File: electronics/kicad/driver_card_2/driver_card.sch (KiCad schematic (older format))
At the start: 27 parts, among them J1 CONN_10SMD_MALE, Q1 2N7002, Q2 MMBT4401, Q3 BSS84, U2 INA194

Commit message: Isoelectric point data
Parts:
- removed R10: 1k, Resistor_SMD:R_0603_1608Metric, symbol SparkFun-Resistors:RESISTOR0402
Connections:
- wire segments 21 -> 20
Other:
- moved on the sheet: C10, Q3, R16, R17, TP4, U2, U?
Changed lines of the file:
@@
 $EndComp
 Wire Wire Line
-	7950 3650 7950 3350
-Wire Wire Line
-	7550 5200 7550 4800
+	7800 3450 7800 3150
+Wire Wire Line
+	7400 5000 7400 4600
 Wire Wire Line
 	4400 5400 4400 5650
@@
 $EndComp
 Wire Wire Line
-	8150 4500 8450 4500
+	8000 4300 8300 4300
 $Comp
 L SparkFun-PowerSymbols:3.3V #SUPPLY0103
@@
 $EndComp
 Wire Wire Line
-	8150 4500 8150 4800
-Connection ~ 8150 4500
-Wire Wire Line
-	8150 4250 8150 4500
+	8000 4300 8000 4600
+Connection ~ 8000 4300
+Wire Wire Line
+	8000 4050 8000 4300
 $Comp
 L SparkFun-Resistors:RESISTOR0402 R17
 U 1 1 5F09ED98
-P 7950 4800
-F 0 "R17" V 7855 4868 45  0000 L CNN
-F 1 "2.2r" V 7939 4868 45  0000 L CNN
-F 2 "Resistor_SMD:R_0805_2012Metric" H 7950 4950 20  0001 C CNN
-F 3 "" H 7950 4800 60  0001 C CNN
-F 4 " " V 8034 4868 60  0000 L CNN "Field4"
-	1    7950 4800
+P 7800 4600
+F 0 "R17" V 7705 4668 45  0000 L CNN
+F 1 "2.2r" V 7789 4668 45  0000 L CNN
+F 2 "Resistor_SMD:R_0805_2012Metric" H 7800 4750 20  0001 C CNN
+F 3 "" H 7800 4600 60  0001 C CNN
+F 4 " " V 7884 4668 60  0000 L CNN "Field4"
+	1    7800 4600
 	-1   0    0    1
 $EndComp
@@
 L power:GND #PWR0115
 U 1 1 5F0715F5
-P 8250 4050
-F 0 "#PWR0115" H 8250 4050 30  0001 C CNN
-F 1 "GND" H 8250 3980 30  0001 C CNN
-F 2 "" H 8250 4050 50  0001 C CNN
-F 3 "" H 8250 4050 50  0001 C CNN
-	1    8250 4050
+P 8100 3850
+F 0 "#PWR0115" H 8100 3850 30  0001 C CNN
+F 1 "GND" H 8100 3780 30  0001 C CNN
+F 2 "" H 8100 3850 50  0001 C CNN
+F 3 "" H 8100 3850 50  0001 C CNN
+	1    8100 3850
 	0    -1   -1   0
 $EndComp
@@
 L SparkFun-PowerSymbols:3.3V #SUPPLY0102
 U 1 1 5F06F21D
-P 7650 4050
-F 0 "#SUPPLY0102" H 7700 4050 45  0001 L BNN
-F 1 "3.3V" V 7650 4178 45  0000 L CNN
-F 2 "" V 7608 4177 60  0000 L CNN
-F 3 "" H 7650 4050 60  0001 C CNN
-	1    7650 4050
+P 7500 3850
+F 0 "#SUPPLY0102" H 7550 3850 45  0001 L BNN
+F 1 "3.3V" V 7500 3978 45  0000 L CNN
+F 2 "" V 7458 3977 60  0000 L CNN
+F 3 "" H 7500 3850 60  0001 C CNN
+	1    7500 3850
 	0    -1   -1   0
 $EndComp
@@
 L power:GND #PWR0112
 U 1 1 5F06BB87
-P 7650 3750
-F 0 "#PWR0112" H 7650 3750 30  0001 C CNN
-F 1 "GND" H 7650 3680 30  0001 C CNN
-F 2 "" H 7650 3750 50  0001 C CNN
-F 3 "" H 7650 3750 50  0001 C CNN
-	1    7650 3750
+P 7500 3550
+F 0 "#PWR0112" H 7500 3550 30  0001 C CNN
+F 1 "GND" H 7500 3480 30  0001 C CNN
+F 2 "" H 7500 3550 50  0001 C CNN
+F 3 "" H 7500 3550 50  0001 C CNN
+	1    7500 3550
 	-1   0    0    1
 $EndComp
@@
 L SparkFun-Capacitors:4.7UF0603 C10
 U 1 1 5F06AAD3
-P 7650 3950
-F 0 "C10" V 7416 4000 45  0000 C CNN
-F 1 "0.1 uF" V 7500 4000 45  0000 C CNN
-F 2 "0603" H 7650 4200 20  0001 C CNN
-F 3 "" H 7650 3950 50  0001 C CNN
-F 4 "" H 7758 3916 60  0000 L CNN "Field4"
-	1    7650 3950
-	1    0    0    -1
-$EndComp
-Wire Wire Line
-	7750 4250 7850 4250
-Wire Wire Line
-	8150 4250 8050 4250
-Connection ~ 7650 4050
+P 7500 3750
+F 0 "C10" V 7266 3800 45  0000 C CNN
+F 1 "0.1 uF" V 7350 3800 45  0000 C CNN
+F 2 "0603" H 7500 4000 20  0001 C CNN
+F 3 "" H 7500 3750 50  0001 C CNN
+F 4 "" H 7608 3716 60  0000 L CNN "Field4"
+	1    7500 3750
+	1    0    0    -1
+$EndComp
+Wire Wire Line
+	7600 4050 7700 4050
+Wire Wire Line
+	8000 4050 7900 4050
+Connection ~ 7500 3850
 $Comp
 L Amplifier_Current:INA194 U2
 U 1 1 5F064800
-P 7950 3950
-F 0 "U2" H 8294 3996 50  0000 L CNN
-F 1 "INA194" H 8294 3905 50  0000 L CNN
-F 2 "Package_TO_SOT_SMD:SOT-23-5" H 7950 3950 50  0001 C CNN
-F 3 "http://www.ti.com/lit/ds/symlink/ina193.pdf" H 7950 3950 50  0001 C CNN
-	1    7950 3950
+P 7800 3750
+F 0 "U2" H 8144 3796 50  0000 L CNN
+F 1 "INA194" H 8144 3705 50  0000 L CNN
+F 2 "Package_TO_SOT_SMD:SOT-23-5" H 7800 3750 50  0001 C CNN
+F 3 "http://www.ti.com/lit/ds/symlink/ina193.pdf" H 7800 3750 50  0001 C CNN
+	1    7800 3750
 	0    -1   -1   0
 $EndComp
@@
 $EndComp
 Wire Wire Line
-	7750 4800 7750 4500
-Wire Wire Line
-	7750 4500 7750 4250
-Connection ~ 7750 4500
+	7600 4600 7600 4300
+Wire Wire Line
+	7600 4300 7600 4050
+Connection ~ 7600 4300
 $Comp
 L SparkFun-Resistors:RESISTOR0402 R16
 U 1 1 5F048AA5
-P 7950 4500
-F 0 "R16" V 7855 4568 45  0000 L CNN
-F 1 "2.2r" V 7939 4568 45  0000 L CNN
-F 2 "Resistor_SMD:R_0805_2012Metric" H 7950 4650 20  0001 C CNN
-F 3 "" H 7950 4500 60  0001 C CNN
-F 4 " " V 8034 4568 60  0000 L CNN "Field4"
-	1    7950 4500
+P 7800 4300
+F 0 "R16" V 7705 4368 45  0000 L CNN
+F 1 "2.2r" V 7789 4368 45  0000 L CNN
+F 2 "Resistor_SMD:R_0805_2012Metric" H 7800 4450 20  0001 C CNN
+F 3 "" H 7800 4300 60  0001 C CNN
+F 4 " " V 7884 4368 60  0000 L CNN "Field4"
+	1    7800 4300
 	-1   0    0    1
 $EndComp
@@
 $EndComp
 Connection ~ 6450 1800
-$Comp
-L SparkFun-Resistors:RESISTOR0402 R10
-U 1 1 5EF918DB
-P 6250 1800
-F 0 "R10" V 6345 1732 45  0000 R CNN
-F 1 "1k" V 6261 1732 45  0000 R CNN
-F 2 "Resistor_SMD:R_0603_1608Metric" H 6250 1950 20  0001 C CNN
-F 3 "" H 6250 1800 60  0001 C CNN
-F 4 " " V 6166 1732 60  0000 R CNN "Field4"
-	1    6250 1800
-	-1   0    0    1
-$EndComp
-Wire Wire Line
-	5900 1800 6050 1800
 Connection ~ 5900 1800
 Connection ~ 6800 2200
@@
 	1    0    0    -1
 $EndComp
-Text GLabel 8500 4500 2    50   Input ~ 0
+Text GLabel 8350 4300 2    50   Input ~ 0
 nsource
 $Comp
 L Transistor_FET:BSS84 Q3
 U 1 1 5EFA7A24
-P 7550 4600
-F 0 "Q3" H 7756 4646 50  0000 L CNN
-F 1 "BSS84" H 7756 4555 50  0000 L CNN
-F 2 "Package_TO_SOT_SMD:SOT-23" H 7750 4525 50  0001 L CIN
-F 3 "http://assets.nexperia.com/documents/data-sheet/BSS84.pdf" H 7550 4600 50  0001 L CNN
-	1    7550 4600
+P 7400 4400
+F 0 "Q3" H 7606 4446 50  0000 L CNN
+F 1 "BSS84" H 7606 4355 50  0000 L CNN
+F 2 "Package_TO_SOT_SMD:SOT-23" H 7600 4325 50  0001 L CIN
+F 3 "http://assets.nexperia.com/documents/data-sheet/BSS84.pdf" H 7400 4400 50  0001 L CNN
+	1    7400 4400
 	0    1    -1   0
 $EndComp
@@
 Text GLabel 7100 2200 2    50   Input ~ 0
 VARACTOR_FEEDBACK
-Text GLabel 7950 3350 1    50   Input ~ 0
+Text GLabel 7800 3150 1    50   Input ~ 0
 CURRENT_SENSE
 Text GLabel 3350 3050 2    50   Input ~ 0
@@
 	0    -1   -1   0
 $EndComp
-Text GLabel 8450 4700 2    50   Input ~ 0
+Text GLabel 8300 4500 2    50   Input ~ 0
 pulse_feedback
 Wire Wire Line
-	8450 4500 8450 4700
-Connection ~ 8450 4500
-Wire Wire Line
-	8450 4500 8500 4500
+	8300 4300 8300 4500
+Connection ~ 8300 4300
+Wire Wire Line
+	8300 4300 8350 4300
 $Comp
 L SparkFun-Capacitors:4.7UF0603 C2
@@
 L Connector:Test_Point TP4
 U 1 1 5EECA2A9
-P 9600 4550
-F 0 "TP4" H 9658 4668 50  0000 L CNN
-F 1 "Test_Point" H 9658 4577 50  0000 L CNN
-F 2 "TestPoint:TestPoint_Pad_2.0x2.0mm" H 9800 4550 50  0001 C CNN
-F 3 "~" H 9800 4550 50  0001 C CNN
-	1    9600 4550
-	0    1    1    0
-$EndComp
-Text GLabel 9600 4550 0    50   Input ~ 0
+P 9450 4350
+F 0 "TP4" H 9508 4468 50  0000 L CNN
+F 1 "Test_Point" H 9508 4377 50  0000 L CNN
+F 2 "TestPoint:TestPoint_Pad_2.0x2.0mm" H 9650 4350 50  0001 C CNN
+F 3 "~" H 9650 4350 50  0001 C CNN
+	1    9450 4350
+	0    1    1    0
+$EndComp
+Text GLabel 9450 4350 0    50   Input ~ 0
 nsource
 Text Notes 7900 1150 0    50   ~ 0
 We could use an op-amp to provide the feedback \nfor both of these circuits, lessening the load on the Teensy,\nbut whatever
-Wire Wire Line
-	6050 1800 6450 1800
-Connection ~ 6050 1800
 $Comp
 L SparkFun-Capacitors:4.7UF0603 C?
@@
 L dk_PMIC-Gate-Drivers:MCP1416T-E_OT U?
 U 1 1 5EFC2AA9
-P 7150 5300
-F 0 "U?" H 7594 5403 60  0000 L CNN
-F 1 "MCP1416T-E_OT" H 7594 5297 60  0000 L CNN
-F 2 "digikey-footprints:SOT-753" H 7350 5500 60  0001 L CNN
-F 3 "http://www.microchip.com/mymicrochip/filehandler.aspx?ddocname=en536128" H 7350 5600 60  0001 L CNN
-F 4 "MCP1416T-E/OTCT-ND" H 7350 5700 60  0001 L CNN "Digi-Key_PN"
-F 5 "MCP1416T-E/OT" H 7350 5800 60  0001 L CNN "MPN"
-F 6 "Integrated Circuits (ICs)" H 7350 5900 60  0001 L CNN "Category"
-F 7 "PMIC - Gate Drivers" H 7350 6000 60  0001 L CNN "Family"
-F 8 "http://www.microchip.com/mymicrochip/filehandler.aspx?ddocname=en536128" H 7350 6100 60  0001 L CNN "DK_Datasheet_Link"
-F 9 "/product-detail/en/microchip-technology/MCP1416T-E-OT/MCP1416T-E-OTCT-ND/1963940" H 7350 6200 60  0001 L CNN "DK_Detail_Page"
-F 10 "IC MOSFET DVR 1.5A HS SOT23-5" H 7350 6300 60  0001 L CNN "Description"
-F 11 "Microchip Technology" H 7350 6400 60  0001 L CNN "Manufacturer"
-F 12 "Active" H 7350 6500 60  0001 L CNN "Status"
-	1    7150 5300
-	1    0    0    -1
-$EndComp
+P 7000 5100
+F 0 "U?" H 7444 5203 60  0000 L CNN
+F 1 "MCP1416T-E_OT" H 7444 5097 60  0000 L CNN
+F 2 "digikey-footprints:SOT-753" H 7200 5300 60  0001 L CNN
+F 3 "http://www.microchip.com/mymicrochip/filehandler.aspx?ddocname=en536128" H 7200 5400 60  0001 L CNN
+F 4 "MCP1416T-E/OTCT-ND" H 7200 5500 60  0001 L CNN "Digi-Key_PN"
+F 5 "MCP1416T-E/OT" H 7200 5600 60  0001 L CNN "MPN"
+F 6 "Integrated Circuits (ICs)" H 7200 5700 60  0001 L CNN "Category"
+F 7 "PMIC - Gate Drivers" H 7200 5800 60  0001 L CNN "Family"
+F 8 "http://www.microchip.com/mymicrochip/filehandler.aspx?ddocname=en536128" H 7200 5900 60  0001 L CNN "DK_Datasheet_Link"
+F 9 "/product-detail/en/microchip-technology/MCP1416T-E-OT/MCP1416T-E-OTCT-ND/1963940" H 7200 6000 60  0001 L CNN "DK_Detail_Page"
+F 10 "IC MOSFET DVR 1.5A HS SOT23-5" H 7200 6100 60  0001 L CNN "Description"
+F 11 "Microchip Technology" H 7200 6200 60  0001 L CNN "Manufacturer"
+F 12 "Active" H 7200 6300 60  0001 L CNN "Status"
+	1    7000 5100
+	1    0    0    -1
+$EndComp
+Wire Wire Line
+	5900 1800 6450 1800
 $EndSCHEMATC

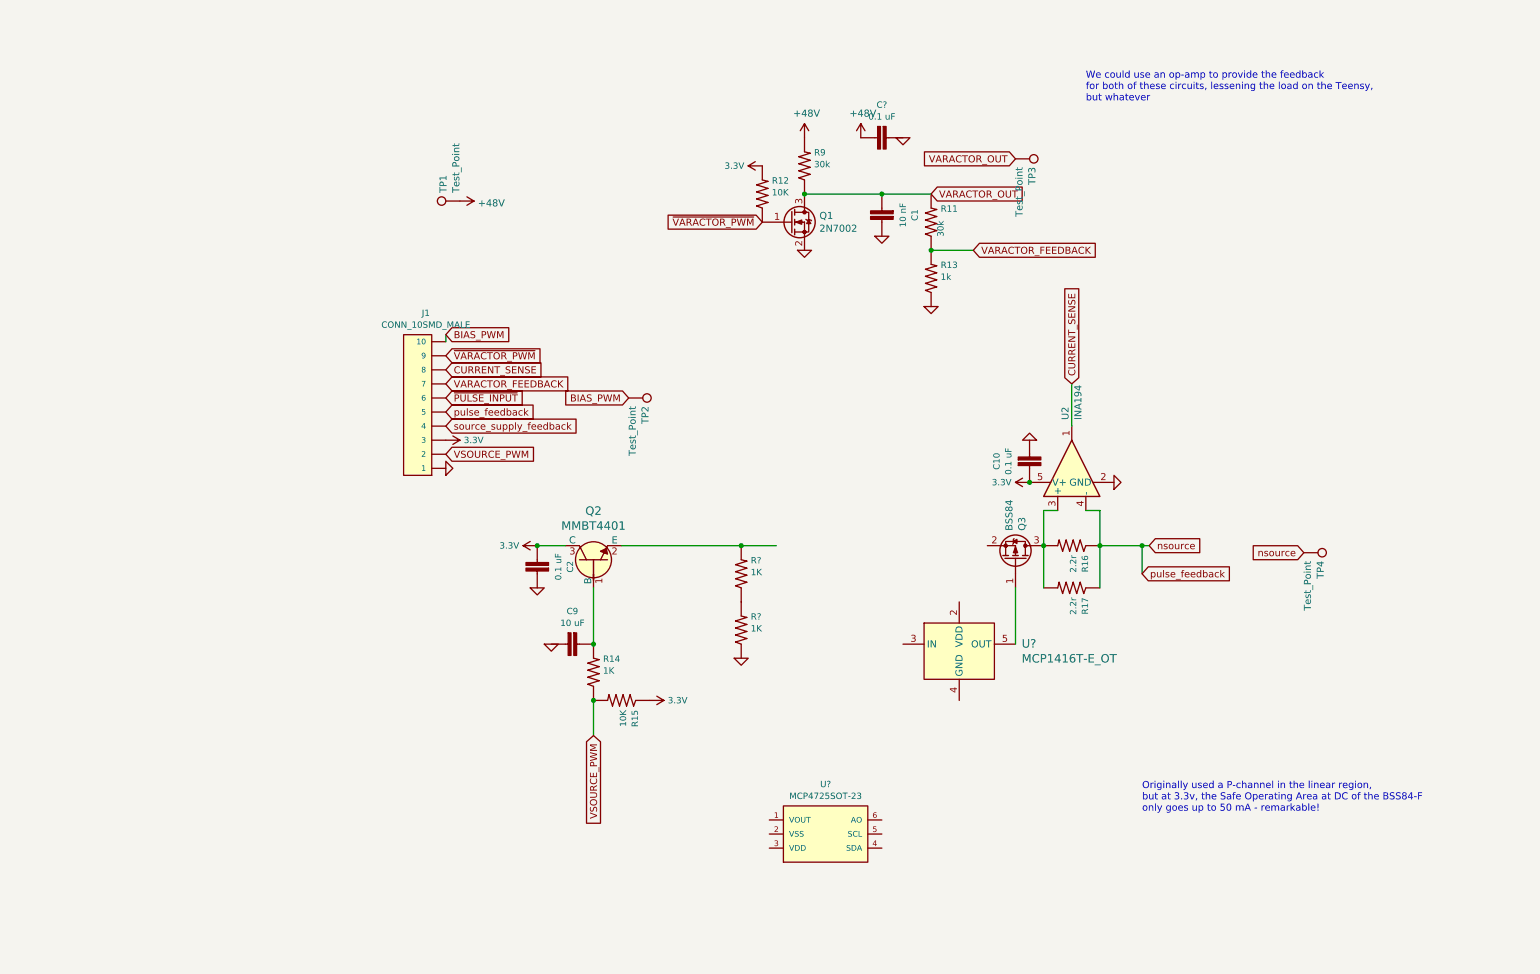
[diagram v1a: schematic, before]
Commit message: Strange oscillations in the amplifier
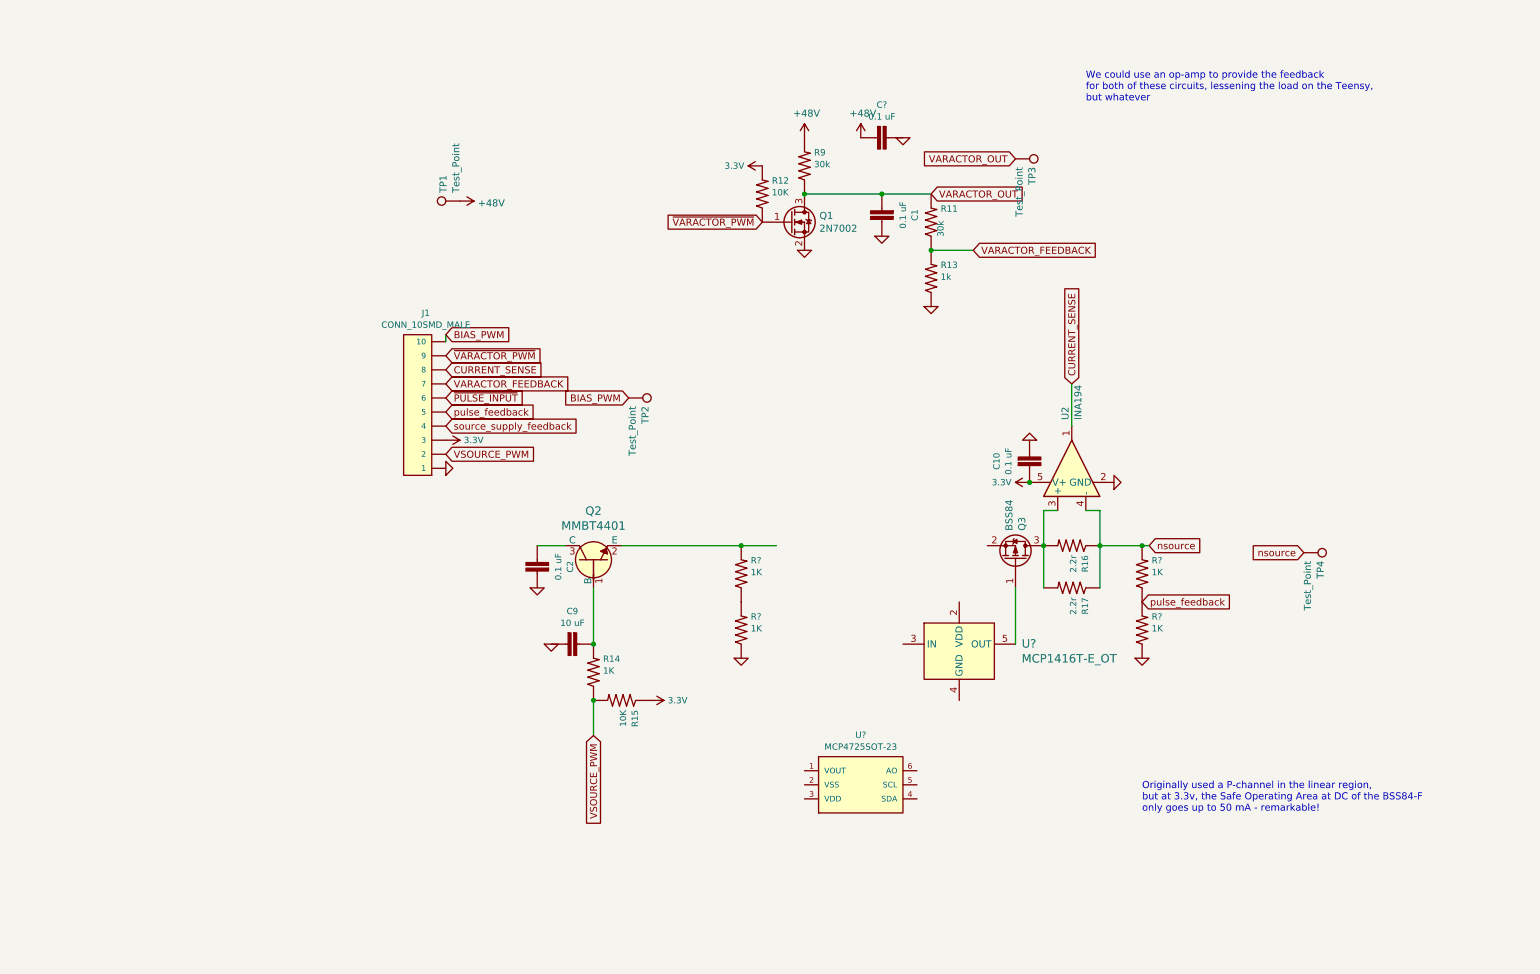
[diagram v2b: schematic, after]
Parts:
- added R? (x2): 1K, Resistor_SMD:R_0402_1005Metric, symbol SparkFun-Resistors:RESISTOR0402
- C1: value 10 nF -> 0.1 uF
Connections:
- wire segments 20 -> 19
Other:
- moved on the sheet: U?
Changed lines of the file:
@@
 P 6450 1900
 F 0 "C1" V 6216 1950 45  0000 C CNN
-F 1 "10 nF" V 6300 1950 45  0000 C CNN
+F 1 "0.1 uF" V 6300 1950 45  0000 C CNN
 F 2 "0603" H 6450 2150 20  0001 C CNN
 F 3 "" H 6450 1900 50  0001 C CNN
@@
 	0    -1   -1   0
 $EndComp
-Wire Wire Line
-	8000 4300 8300 4300
 $Comp
 L SparkFun-PowerSymbols:3.3V #SUPPLY0103
@@
 F 3 "" H 7500 3850 60  0001 C CNN
 	1    7500 3850
-	0    -1   -1   0
-$EndComp
-$Comp
-L SparkFun-PowerSymbols:3.3V #SUPPLY0101
-U 1 1 5F06D0A6
-P 4000 4300
-F 0 "#SUPPLY0101" H 4050 4300 45  0001 L BNN
-F 1 "3.3V" V 4000 4428 45  0000 L CNN
-F 2 "" V 3958 4427 60  0000 L CNN
-F 3 "" H 4000 4300 60  0001 C CNN
-	1    4000 4300
 	0    -1   -1   0
 $EndComp
@@
 	0    -1   -1   0
 $EndComp
-Text GLabel 8300 4500 2    50   Input ~ 0
-pulse_feedback
-Wire Wire Line
-	8300 4300 8300 4500
-Connection ~ 8300 4300
-Wire Wire Line
-	8300 4300 8350 4300
 $Comp
 L SparkFun-Capacitors:4.7UF0603 C2
@@
 	-1   0    0    1
 $EndComp
-Connection ~ 4000 4300
 $Comp
 L power:GND #PWR0102
@@
 L SparkFun-IC-Conversion:MCP4725SOT-23 U?
 U 1 1 5EFD9BA3
-P 6050 6350
-F 0 "U?" H 6050 6704 45  0000 C CNN
-F 1 "MCP4725SOT-23" H 6050 6620 45  0000 C CNN
-F 2 "SOT23-6" H 6050 6650 20  0001 C CNN
-F 3 "" H 6050 6350 50  0001 C CNN
-F 4 "" H 6050 6631 60  0000 C CNN "Field4"
-	1    6050 6350
+P 6300 6000
+F 0 "U?" H 6300 6354 45  0000 C CNN
+F 1 "MCP4725SOT-23" H 6300 6270 45  0000 C CNN
+F 2 "SOT23-6" H 6300 6300 20  0001 C CNN
+F 3 "" H 6300 6000 50  0001 C CNN
+F 4 "" H 6300 6281 60  0000 C CNN "Field4"
+	1    6300 6000
 	1    0    0    -1
 $EndComp
@@
 Wire Wire Line
 	5900 1800 6450 1800
+Text GLabel 8300 4700 2    50   Input ~ 0
+pulse_feedback
+$Comp
+L SparkFun-Resistors:RESISTOR0402 R?
+U 1 1 5EFFA64D
+P 8300 4500
+F 0 "R?" V 8395 4432 45  0000 R CNN
+F 1 "1K" V 8311 4432 45  0000 R CNN
+F 2 "Resistor_SMD:R_0402_1005Metric" H 8300 4650 20  0001 C CNN
+F 3 "" H 8300 4500 60  0001 C CNN
+F 4 " " V 8216 4432 60  0000 R CNN "Field4"
+	1    8300 4500
+	0    -1   -1   0
+$EndComp
+$Comp
+L SparkFun-Resistors:RESISTOR0402 R?
+U 1 1 5EFFA654
+P 8300 4900
+F 0 "R?" V 8395 4832 45  0000 R CNN
+F 1 "1K" V 8311 4832 45  0000 R CNN
+F 2 "Resistor_SMD:R_0402_1005Metric" H 8300 5050 20  0001 C CNN
+F 3 "" H 8300 4900 60  0001 C CNN
+F 4 " " V 8216 4832 60  0000 R CNN "Field4"
+	1    8300 4900
+	0    -1   -1   0
+$EndComp
+$Comp
+L power:GND #PWR?
+U 1 1 5EFFA65A
+P 8300 5100
+F 0 "#PWR?" H 8300 5100 30  0001 C CNN
+F 1 "GND" H 8300 5030 30  0001 C CNN
+F 2 "" H 8300 5100 50  0001 C CNN
+F 3 "" H 8300 5100 50  0001 C CNN
+	1    8300 5100
+	1    0    0    -1
+$EndComp
+Wire Wire Line
+	8000 4300 8300 4300
+Connection ~ 8300 4300
+Wire Wire Line
+	8300 4300 8350 4300
 $EndSCHEMATC

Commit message: Spectrum analyzer progress
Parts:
- removed Q2: MMBT4401, digikey-footprints:SOT-23-3, symbol dk_Transistors-Bipolar-BJT-Single:MMBT4401
- removed R11: 30k, Resistor_SMD:R_0603_1608Metric, symbol SparkFun-Resistors:RESISTOR0402
- removed R? (x3): 1K, Resistor_SMD:R_0402_1005Metric, symbol SparkFun-Resistors:RESISTOR0402
- added C11, C8: 0.1 uF, 0603, symbol SparkFun-Capacitors:4.7UF0603
- added C4: 10 uF, 0603, symbol SparkFun-Capacitors:4.7UF0603
- added C5, C6, C7: 10uF, 1206, symbol SparkFun-Capacitors:10UF-1206-6.3V-20%
- added Q2, Q4: 2N7002, Package_TO_SOT_SMD:SOT-23, symbol Transistor_FET:BSS138
- added R1: 30k, Resistor_SMD:R_0603_1608Metric, symbol SparkFun-Resistors:RESISTOR0402
- added R10, R4: 1K, Resistor_SMD:R_0603_1608Metric, symbol SparkFun-Resistors:RESISTOR0402
- added R11: 30k, Resistor_SMD:R_0603_1608Metric, symbol SparkFun-Resistors:0.05OHM-0603-1_5W-1%
- added R18: 10k, Resistor_SMD:R_0603_1608Metric, symbol SparkFun-Resistors:0.05OHM-0603-1_5W-1%
- added R19, R2: 10k, Resistor_SMD:R_0603_1608Metric, symbol SparkFun-Resistors:RESISTOR0402
- added R3, R7: 5k, Resistor_SMD:R_0603_1608Metric, symbol SparkFun-Resistors:RESISTOR0402
- added R5, R6: 2k, Resistor_SMD:R_0603_1608Metric, symbol SparkFun-Resistors:RESISTOR0402
- added U3: AZ1117CH-3_3TRG1, digikey-footprints:SOT-223, symbol dk_PMIC-Voltage-Regulators-Linear:AZ1117CH-3_3TRG1
- R12: value 10K -> 1k
- R14: value 1K -> 1k; footprint Resistor_SMD:R_0402_1005Metric -> Resistor_SMD:R_0603_1608Metric
- R15: value 10K -> 1k; footprint Resistor_SMD:R_0402_1005Metric -> Resistor_SMD:R_0603_1608Metric
- R16: value 2.2r -> 0.1R
- R17: value 2.2r -> 1k; footprint Resistor_SMD:R_0805_2012Metric -> Resistor_SMD:R_0603_1608Metric
- R8: renamed from R?; value 1K -> 5k; footprint Resistor_SMD:R_0402_1005Metric -> Resistor_SMD:R_0603_1608Metric
- TP1: value Test_Point -> 48V
- TP2: value Test_Point -> 12V
- gave numbers to parts that had none: 3
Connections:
- net labels added: +12V, BIAS_OUT, ~VARACTOR_INPUT
- wire segments 19 -> 28
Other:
- note added: "Originally used a P-channel in the linear region,\nbut, surprisingly, at 3.3v, the Safe Operating Area at DC of the BSS84-F \nonly goes up to 50 mA."
- note removed: "Originally used a P-channel in the linear region,\nbut at 3.3v, the Safe Operating Area at DC of the BSS84-F \nonly goes up to 50 mA - remarkable!"
- note removed: "We could use an op-amp to provide the feedback \nfor both of these circuits, lessening the load on the Teensy,\nbut whatever"
- moved on the sheet: C10, C2, C3, J1, Q3, R16, R8, TP1, TP3, TP4, U1, U2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
